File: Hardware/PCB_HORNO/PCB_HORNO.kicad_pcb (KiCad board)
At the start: 2 copper layers, 269 parts, among them J0_1 Screw_Terminal_01x03, J0_10 Screw_Terminal_01x03, J0_11 Screw_Terminal_01x03, J0_12 Screw_Terminal_01x03, J0_13 Screw_Terminal_01x03, J0_14 Screw_Terminal_01x03, J0_15 Screw_Terminal_01x03, J0_16 Screw_Terminal_01x03, J0_2 Screw_Terminal_01x03, J0_3 Screw_Terminal_01x03, J0_4 Screw_Terminal_01x03, J0_5 Screw_Terminal_01x03, J0_6 Screw_Terminal_01x03, J0_7 Screw_Terminal_01x03, J0_8 Screw_Terminal_01x03, J0_9 Screw_Terminal_01x03, J1 Screw_Terminal_01x20, J2 Screw_Terminal_01x20, J3 Screw_Terminal_01x20, J4 Screw_Terminal_01x20, J9_1 Screw_Terminal_01x03, J9_5 Screw_Terminal_01x03, Q1 2N2222, Q10 IRG4PF50W, Q2 2N2222, Q3 2N2222, Q4 2N2222, Q5 BTA16-800B, U1 TLP521-1, U10 LM741, U11 LM741, U12 LM741, U13 MOC3021M, U14 TLP521-1, U15 4069, U16 LM741, U17 LM741, U18 LM741, U19 TLP250, U2 TLP521-1, U20 L298HN, U21 4069, U3 TLP521-1, U4 TLP521-1, U5 TLP521-1, U6 TLP521-1, U7 TLP521-1, U8 TLP521-1, U9 LM741

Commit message: Esquematico listo
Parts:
- removed D9: D_Bridge_+-AA, Diode_THT:Diode_Bridge_19.0x3.5x10.0mm_P5.0mm
- removed the J0_14 at (-42.6, 357.2)
- removed the J0_14 at (243.4, 362.3)
- removed PX100, PX101, PX102, PX103, PX104, PX105, PX106, PX107, PX108, PX109, PX110, PX63, PX64, PX65, PX66, PX67, PX68, PX69, PX70, PX71, PX72, PX73, PX74, PX75, PX76, PX77, PX78, PX79, PX80, PX81, PX82, PX83, PX84, PX85, PX86, PX87, PX88, PX89, PX90, PX91, PX92, PX93, PX94, PX95, PX96, PX97, PX98, PX99: ~, Connector_Wire:SolderWire-0.75sqmm_1x01_D1.25mm_OD2.3mm
- removed U15, U21: 4069, Package_TO_SOT_SMD:SOT-353_SC-70-5
- added C10: 100nF, Capacitor_THT:C_Disc_D5.1mm_W3.2mm_P5.00mm, F.Cu at (152.8, 399.2)
- added C11: 100nF, Capacitor_THT:C_Disc_D5.1mm_W3.2mm_P5.00mm, F.Cu at (152.8, 404.0)
- added D10: GBU8J, Diode_THT:Diode_Bridge_Vishay_GBU, F.Cu at (-160.2, 414.6)
- added J0_14: Screw_Terminal_01x03, TerminalBlock_Phoenix:TerminalBlock_Phoenix_PT-1,5-3-3.5-H_1x03_P3.50mm_Horizontal, F.Cu at (247.8, 410.9)
- C1, C2, C3, C4, C5, C6, C7, C8, C9: footprint Capacitor_THT:C_Disc_D4.3mm_W1.9mm_P5.00mm -> Capacitor_THT:C_Disc_D5.1mm_W3.2mm_P5.00mm
- Q1, Q2, Q3, Q4: footprint Package_TO_SOT_THT:TO-39-3 -> Package_TO_SOT_THT:TO-92
- moved PX45 426.3 mm to (-314.9, 424.2)
- moved PX47 426.3 mm to (-314.9, 433.5)
- moved PX46 426.3 mm to (-314.9, 428.8)
- moved PX53 426.1 mm to (-305.2, 433.5)
- moved PX48 416.0 mm to (-310.1, 424.2)
- moved PX49 416.0 mm to (-310.1, 428.8)
- moved PX50 416.0 mm to (-310.1, 433.5)
- moved PX51 406.0 mm to (-305.2, 424.2)
- moved PX52 406.0 mm to (-305.2, 428.8)
- moved PX120 393.8 mm to (575.5, 400.5)
- moved PX121 393.8 mm to (575.5, 405.2)
- moved PX122 393.8 mm to (575.5, 409.8)
- moved PX123 393.8 mm to (575.5, 414.5)
- moved PX124 393.8 mm to (575.5, 419.1)
- moved PX54 286.0 mm to (-151.2, 420.0)
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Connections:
- C1 pad 1: unconnected-(C1-Pad1) -> Net-(3V3a1-Pin_1)
- C1 pad 2: unconnected-(C1-Pad2) -> Net-(GND1-Pin_1)
- C2 pad 1: unconnected-(C2-Pad1) -> Net-(3V3b1-Pin_1)
- C2 pad 2: unconnected-(C2-Pad2) -> Net-(GND3-Pin_1)
- C3 pad 1: Net-(J0_6-Pin_1) -> Net-(U12-+)
- C7 pad 1: Net-(U16-+) -> Net-(PX117-Pin_1)
- C7 pad 2: Net-(C7-Pad2) -> Net-(J0_12-Pin_3)
- C8 pad 1: Net-(U17-+) -> Net-(PX118-Pin_1)
- C8 pad 2: Net-(C7-Pad2) -> Net-(J0_12-Pin_3)
- C9 pad 1: Net-(U18-+) -> Net-(PX119-Pin_1)
- C9 pad 2: Net-(C7-Pad2) -> Net-(J0_12-Pin_3)
- J0_12 pad 2: unconnected-(J0_12-Pin_2-Pad2) -> Net-(J0_12-Pin_2)
- J0_6 pad 1: Net-(J0_6-Pin_1) -> unconnected-(J0_6-Pin_1-Pad1)
- J0_6 pad 2: unconnected-(J0_6-Pin_2-Pad2) -> Net-(J0_4-Pin_1)
- J0_6 pad 3: unconnected-(J0_6-Pin_3-Pad3) -> Net-(J0_4-Pin_1)
- PX111 pad 1: unconnected-(PX111-Pin_1-Pad1) -> Net-(PX111-Pin_1)
- PX112 pad 1: unconnected-(PX112-Pin_1-Pad1) -> Net-(PX112-Pin_1)
- PX113 pad 1: unconnected-(PX113-Pin_1-Pad1) -> Net-(PX113-Pin_1)
- PX114 pad 1: unconnected-(PX114-Pin_1-Pad1) -> Net-(PX114-Pin_1)
- PX115 pad 1: unconnected-(PX115-Pin_1-Pad1) -> Net-(PX115-Pin_1)
- PX116 pad 1: unconnected-(PX116-Pin_1-Pad1) -> Net-(J0_12-Pin_3)
- PX117 pad 1: unconnected-(PX117-Pin_1-Pad1) -> Net-(PX117-Pin_1)
- PX118 pad 1: unconnected-(PX118-Pin_1-Pad1) -> Net-(PX118-Pin_1)
- PX119 pad 1: unconnected-(PX119-Pin_1-Pad1) -> Net-(PX119-Pin_1)
- PX120 pad 1: unconnected-(PX120-Pin_1-Pad1) -> Net-(J0_4-Pin_1)
- PX121 pad 1: unconnected-(PX121-Pin_1-Pad1) -> Net-(PX121-Pin_1)
- PX122 pad 1: unconnected-(PX122-Pin_1-Pad1) -> Net-(PX122-Pin_1)
- PX123 pad 1: unconnected-(PX123-Pin_1-Pad1) -> Net-(PX123-Pin_1)
- PX124 pad 1: unconnected-(PX124-Pin_1-Pad1) -> Net-(PX124-Pin_1)
- PX45 pad 1: unconnected-(PX45-Pin_1-Pad1) -> Net-(J9_1-Pin_1)
- PX46 pad 1: unconnected-(PX46-Pin_1-Pad1) -> Net-(J9_1-Pin_1)
- PX47 pad 1: unconnected-(PX47-Pin_1-Pad1) -> Net-(PX47-Pin_1)
- PX48 pad 1: unconnected-(PX48-Pin_1-Pad1) -> Net-(PX48-Pin_1)
- PX49 pad 1: unconnected-(PX49-Pin_1-Pad1) -> Net-(PX49-Pin_1)
- PX50 pad 1: unconnected-(PX50-Pin_1-Pad1) -> Net-(PX50-Pin_1)
- PX51 pad 1: unconnected-(PX51-Pin_1-Pad1) -> Net-(PX51-Pin_1)
- PX52 pad 1: unconnected-(PX52-Pin_1-Pad1) -> Net-(PX52-Pin_1)
- PX53 pad 1: unconnected-(PX53-Pin_1-Pad1) -> Net-(PX53-Pin_1)
- PX54 pad 1: unconnected-(PX54-Pin_1-Pad1) -> Net-(PX54-Pin_1)
- PX55 pad 1: unconnected-(PX55-Pin_1-Pad1) -> Net-(J0_11-Pin_3)
- PX56 pad 1: unconnected-(PX56-Pin_1-Pad1) -> Net-(PX56-Pin_1)
- PX57 pad 1: unconnected-(PX57-Pin_1-Pad1) -> Net-(PX57-Pin_1)
- PX58 pad 1: unconnected-(PX58-Pin_1-Pad1) -> Net-(PX58-Pin_1)
- PX59 pad 1: unconnected-(PX59-Pin_1-Pad1) -> Net-(PX59-Pin_1)
- PX60 pad 1: unconnected-(PX60-Pin_1-Pad1) -> Net-(PX60-Pin_1)
- PX61 pad 1: unconnected-(PX61-Pin_1-Pad1) -> Net-(J0_16-Pin_1)
- PX62 pad 1: unconnected-(PX62-Pin_1-Pad1) -> Net-(PX62-Pin_1)
- Q1 pad 1: Net-(Q1-E) -> Net-(PX124-Pin_1)
- Q2 pad 1: Net-(Q2-E) -> Net-(PX123-Pin_1)
- Q3 pad 1: Net-(Q3-E) -> Net-(PX122-Pin_1)
- Q4 pad 1: Net-(Q4-E) -> Net-(PX121-Pin_1)
- R12 pad 1: Net-(R12-Pad1) -> Net-(J0_11-Pin_1)
- R12 pad 2: Net-(J0_11-Pin_3) -> Net-(PX54-Pin_1)
- R18 pad 1: unconnected-(R18-Pad1) -> Net-(PX57-Pin_1)
- R19 pad 2: Net-(C7-Pad2) -> Net-(J0_12-Pin_3)
- R2 pad 1: Net-(R2-Pad1) -> Net-(PX47-Pin_1)
- R21 pad 2: Net-(C7-Pad2) -> Net-(J0_12-Pin_3)
- R23 pad 2: Net-(C7-Pad2) -> Net-(J0_12-Pin_3)
- R25 pad 2: unconnected-(R25-Pad2) -> Net-(PX115-Pin_1)
- R3 pad 1: Net-(R3-Pad1) -> Net-(PX48-Pin_1)
- R35 pad 1: Net-(Q4-E) -> Net-(PX121-Pin_1)
- R36 pad 1: Net-(Q3-E) -> Net-(PX122-Pin_1)
- R37 pad 1: Net-(Q2-E) -> Net-(PX123-Pin_1)
- R38 pad 1: Net-(Q1-E) -> Net-(PX124-Pin_1)
- R39 pad 1: unconnected-(R39-Pad1) -> Net-(J0_16-Pin_1)
- R4 pad 1: Net-(R4-Pad1) -> Net-(PX49-Pin_1)
- R40 pad 1: unconnected-(R40-Pad1) -> Net-(J0_16-Pin_1)
- R5 pad 1: Net-(R5-Pad1) -> Net-(PX50-Pin_1)
- R6 pad 1: Net-(R6-Pad1) -> Net-(PX51-Pin_1)
- R7 pad 1: Net-(R7-Pad1) -> Net-(PX52-Pin_1)
- R8 pad 1: Net-(R8-Pad1) -> Net-(PX53-Pin_1)
- RV1 pad 1: unconnected-(RV1-Pad1) -> Net-(PX58-Pin_1)
- RV1 pad 2: unconnected-(RV1-Pad2) -> Net-(PX59-Pin_1)
- RV1 pad 3: unconnected-(RV1-Pad3) -> Net-(PX60-Pin_1)
- U12 pad 3: Net-(J0_6-Pin_1) -> Net-(U12-+)
- U13 pad 2: unconnected-(U13-Pad2) -> Net-(PX56-Pin_1)
- U14 pad 3: Net-(J0_11-Pin_1) -> Net-(J0_11-Pin_3)
- U14 pad 4: Net-(R12-Pad1) -> Net-(PX54-Pin_1)
- U16 pad 3: Net-(U16-+) -> Net-(PX117-Pin_1)
- U16 pad 4: Net-(J0_12-Pin_3) -> Net-(J0_12-Pin_1)
- U16 pad 7: Net-(J0_12-Pin_1) -> Net-(J0_12-Pin_2)
- U17 pad 3: Net-(U17-+) -> Net-(PX118-Pin_1)
- U17 pad 4: Net-(J0_12-Pin_3) -> Net-(J0_12-Pin_1)
- U17 pad 7: Net-(J0_12-Pin_1) -> Net-(J0_12-Pin_2)
- U18 pad 3: Net-(U18-+) -> Net-(PX119-Pin_1)
- U18 pad 4: Net-(J0_12-Pin_3) -> Net-(J0_12-Pin_1)
- U18 pad 7: Net-(J0_12-Pin_1) -> Net-(J0_12-Pin_2)
- U19 pad 3: unconnected-(U19-C-Pad3) -> Net-(PX114-Pin_1)
- U2 pad 3: Net-(R2-Pad1) -> Net-(PX47-Pin_1)
- U20 pad 10: Net-(U20-IN3) -> Net-(PX111-Pin_1)
- U20 pad 12: Net-(U20-IN4) -> Net-(PX62-Pin_1)
- U20 pad 5: Net-(U20-IN1) -> Net-(PX113-Pin_1)
- U20 pad 7: Net-(U20-IN2) -> Net-(PX112-Pin_1)
- U3 pad 3: Net-(R3-Pad1) -> Net-(PX48-Pin_1)
- U4 pad 3: Net-(R4-Pad1) -> Net-(PX49-Pin_1)
- U5 pad 3: Net-(R5-Pad1) -> Net-(PX50-Pin_1)
- U6 pad 3: Net-(R6-Pad1) -> Net-(PX51-Pin_1)
- U7 pad 3: Net-(R7-Pad1) -> Net-(PX52-Pin_1)
- U8 pad 3: Net-(R8-Pad1) -> Net-(PX53-Pin_1)

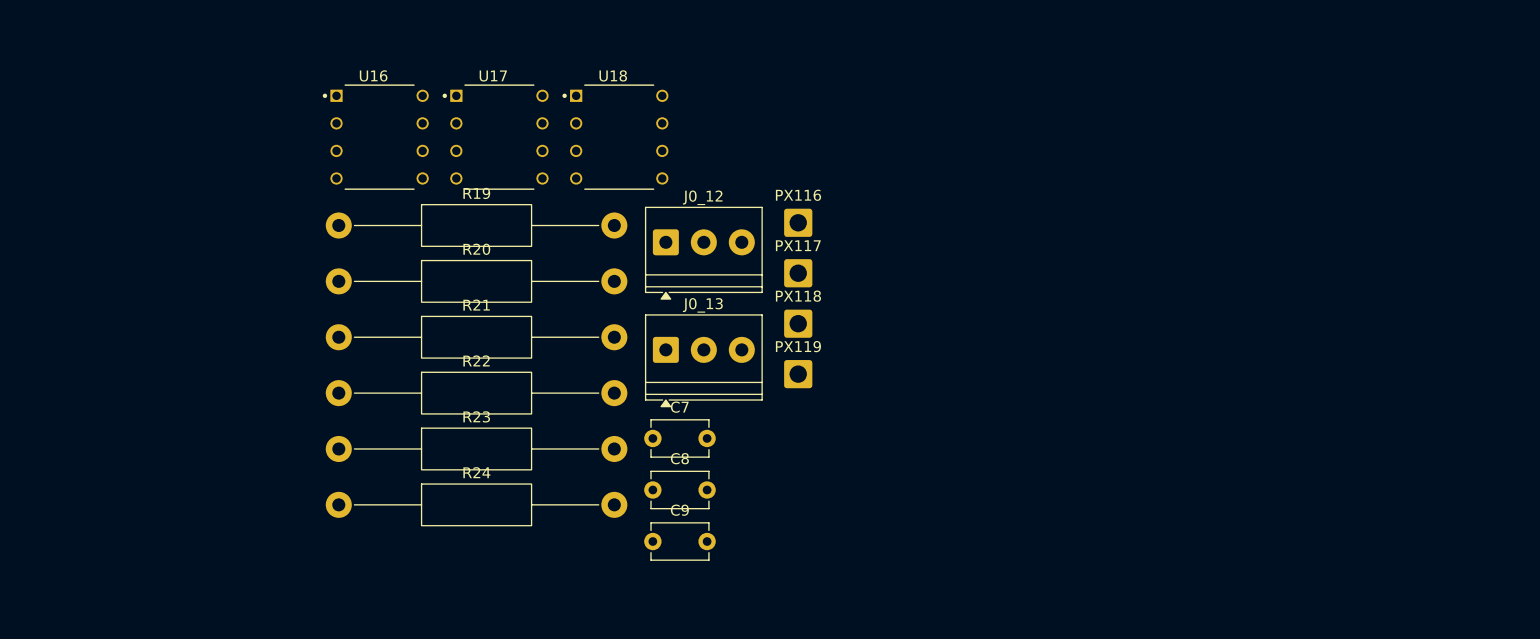
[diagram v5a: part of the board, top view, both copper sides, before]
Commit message: Reorganización del esquematico
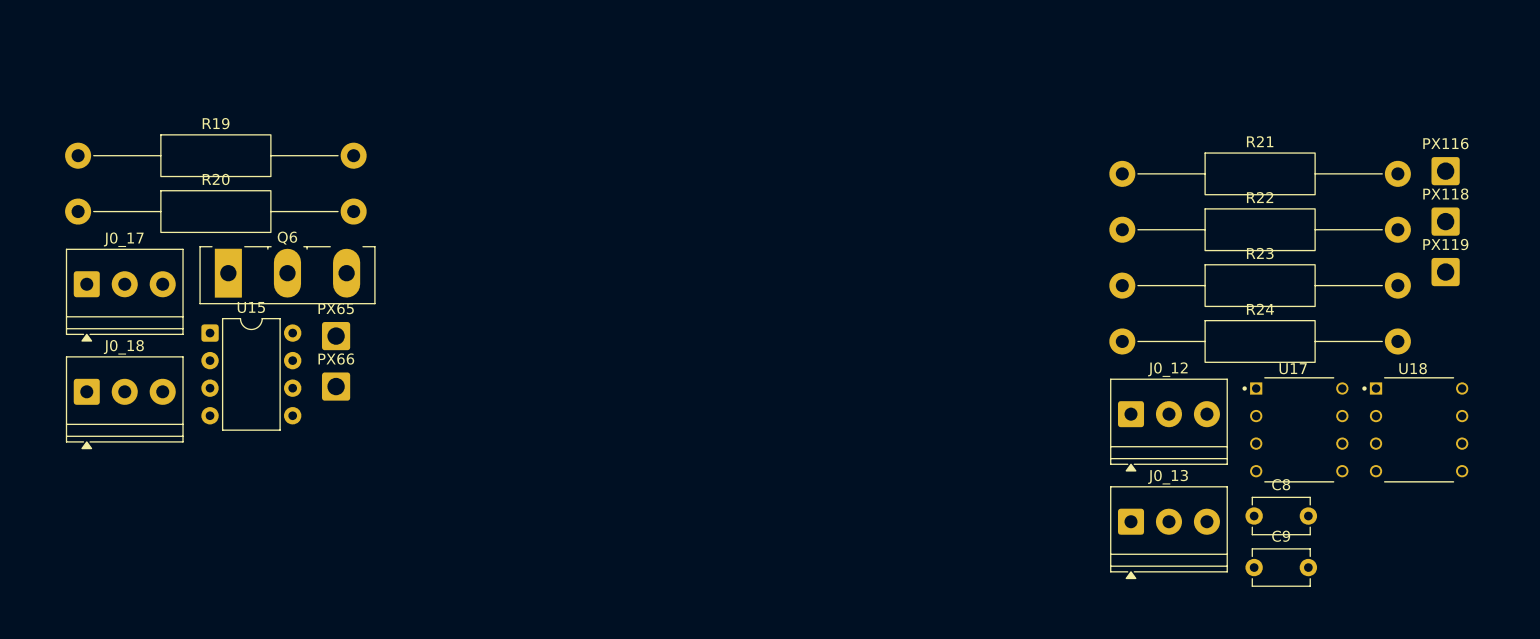
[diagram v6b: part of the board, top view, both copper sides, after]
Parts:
- removed C7: 10nF, Capacitor_THT:C_Disc_D5.1mm_W3.2mm_P5.00mm
- removed PX117: ~, Connector_Wire:SolderWire-0.75sqmm_1x01_D1.25mm_OD2.3mm
- removed U16: LM741, LM741_TH:LM471_TH
- added J0_17: Screw_Terminal_01x03, TerminalBlock_Phoenix:TerminalBlock_Phoenix_PT-1,5-3-3.5-H_1x03_P3.50mm_Horizontal, F.Cu at (340.4, 409.2)
- added J0_18: Screw_Terminal_01x03, TerminalBlock_Phoenix:TerminalBlock_Phoenix_PT-1,5-3-3.5-H_1x03_P3.50mm_Horizontal, F.Cu at (340.4, 419.1)
- added PX65: ~, Connector_Wire:SolderWire-0.75sqmm_1x01_D1.25mm_OD2.3mm, F.Cu at (363.4, 413.9)
- added PX66: ~, Connector_Wire:SolderWire-0.75sqmm_1x01_D1.25mm_OD2.3mm, F.Cu at (363.4, 418.6)
- added Q6: IRG4PF50W, Package_TO_SOT_THT:TO-247-3_Vertical, F.Cu at (353.5, 408.1)
- added U15: TLP250, Package_DIP:DIP-8_W7.62mm, F.Cu at (351.8, 413.7)
- moved U17 78.5 mm to (452.2, 422.6)
- moved U18 78.5 mm to (463.2, 422.6)
- moved R21 73.8 mm to (435.9, 399.0)
- moved R22 73.8 mm to (435.9, 404.1)
- moved R23 73.8 mm to (435.9, 409.3)
- moved R24 73.8 mm to (435.9, 414.4)
- moved PX118 60.4 mm to (465.7, 403.4)
- moved PX119 60.4 mm to (465.7, 408.0)
- moved PX116 59.9 mm to (465.7, 398.7)
- moved C8 55.5 mm to (448.0, 430.5)
- moved C9 55.5 mm to (448.0, 435.3)
- moved J0_12 45.7 mm to (436.7, 421.1)
- moved J0_13 45.7 mm to (436.7, 431.1)
- moved R19 24.9 mm to (339.6, 397.3)
- moved R20 24.9 mm to (339.6, 402.5)
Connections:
- C3 pad 1: Net-(U12-+) -> Net-(J0_6-Pin_1)
- C8 pad 2: Net-(J0_12-Pin_3) -> Net-(C8-Pad2)
- C9 pad 2: Net-(J0_12-Pin_3) -> Net-(C8-Pad2)
- J0_13 pad 2: Net-(J0_13-Pin_2) -> unconnected-(J0_13-Pin_2-Pad2)
- J0_6 pad 1: unconnected-(J0_6-Pin_1-Pad1) -> Net-(J0_6-Pin_1)
- R19 pad 1: Net-(U16--) -> Net-(Q6-G)
- R19 pad 2: Net-(J0_12-Pin_3) -> Net-(R19-Pad2)
- R20 pad 1: Net-(J0_13-Pin_3) -> Net-(U15-A)
- R20 pad 2: Net-(U16--) -> Net-(PX66-Pin_1)
- R21 pad 2: Net-(J0_12-Pin_3) -> Net-(C8-Pad2)
- R22 pad 1: Net-(J0_13-Pin_2) -> Net-(J0_13-Pin_3)
- R23 pad 2: Net-(J0_12-Pin_3) -> Net-(C8-Pad2)
- U12 pad 3: Net-(U12-+) -> Net-(J0_6-Pin_1)
- U17 pad 6: Net-(J0_13-Pin_2) -> Net-(J0_13-Pin_3)

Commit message: Organizando elementos en PCB
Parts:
- added J0_19: Screw_Terminal_01x03, TerminalBlock_Phoenix:TerminalBlock_Phoenix_PT-1,5-3-3.5-H_1x03_P3.50mm_Horizontal, F.Cu at (169.6, 323.4)
- added J0_20: Screw_Terminal_01x03, TerminalBlock_Phoenix:TerminalBlock_Phoenix_PT-1,5-3-3.5-H_1x03_P3.50mm_Horizontal, F.Cu at (153.9, 323.4)
- added PX63: ~, Connector_Wire:SolderWire-0.75sqmm_1x01_D1.25mm_OD2.3mm, F.Cu at (162.8, 261.2)
- added PX64: ~, Connector_Wire:SolderWire-0.75sqmm_1x01_D1.25mm_OD2.3mm, F.Cu at (158.2, 261.2)
- added PX67: ~, Connector_Wire:SolderWire-0.75sqmm_1x01_D1.25mm_OD2.3mm, F.Cu at (153.5, 261.2)
- added PX68: ~, Connector_Wire:SolderWire-0.75sqmm_1x01_D1.25mm_OD2.3mm, F.Cu at (176.8, 261.2)
- added PX69: ~, Connector_Wire:SolderWire-0.75sqmm_1x01_D1.25mm_OD2.3mm, F.Cu at (172.2, 261.2)
- added PX70: ~, Connector_Wire:SolderWire-0.75sqmm_1x01_D1.25mm_OD2.3mm, F.Cu at (167.5, 261.2)
- Q10, Q6: footprint Package_TO_SOT_THT:TO-247-3_Vertical -> Package_TO_SOT_THT:TO-264-3_Vertical
- RV1: value R_Potentiometer_US -> Potentiometer
- moved PX66 182.7 mm to (269.6, 261.8), turned to 90 degrees
- moved PX113 182.3 mm to (84.9, 261.3), turned to 90 degrees
- moved PX65 181.2 mm to (265.0, 261.8), turned to 90 degrees
- moved PX112 180.1 mm to (80.2, 261.3), turned to 90 degrees
- moved PX111 178.0 mm to (75.6, 261.3), turned to 90 degrees
- moved PX62 176.2 mm to (71.0, 261.3), turned to 90 degrees
- moved PX61 174.6 mm to (66.3, 261.3), turned to 90 degrees
- moved PX115 166.4 mm to (219.2, 262.1), turned to 90 degrees
- moved PX114 163.5 mm to (214.5, 262.1), turned to 90 degrees
- moved U20 157.1 mm to (98.6, 276.2), turned to -90 degrees
- moved PX60 156.7 mm to (13.0, 261.3), turned to -90 degrees
- moved PX57 155.8 mm to (-53.9, 261.3), turned to 90 degrees
- moved PX56 152.0 mm to (-58.5, 261.3), turned to 90 degrees
- moved PX59 151.5 mm to (17.6, 261.3), turned to -90 degrees
- moved PX58 146.3 mm to (22.3, 261.3), turned to -90 degrees
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
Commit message: Actualización de esquematico
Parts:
- removed J0_11, J0_12, J0_15, J0_17, J0_4, J9_1, J9_5: Screw_Terminal_01x03, TerminalBlock_Phoenix:TerminalBlock_Phoenix_PT-1,5-3-3.5-H_1x03_P3.50mm_Horizontal
- removed PX114, PX115: ~, Connector_Wire:SolderWire-0.75sqmm_1x01_D1.25mm_OD2.3mm
- removed Q10: IRG4PF50W, Package_TO_SOT_THT:TO-264-3_Vertical
- added J0_21: Screw_Terminal_01x03, TerminalBlock_Phoenix:TerminalBlock_Phoenix_PT-1,5-3-3.5-H_1x03_P3.50mm_Horizontal, F.Cu at (115.0, 427.5)
- added J0_22: Screw_Terminal_01x03, TerminalBlock_Phoenix:TerminalBlock_Phoenix_PT-1,5-3-3.5-H_1x03_P3.50mm_Horizontal, F.Cu at (115.0, 437.4)
- added J0_23: Screw_Terminal_01x03, TerminalBlock_Phoenix:TerminalBlock_Phoenix_PT-1,5-3-3.5-H_1x03_P3.50mm_Horizontal, F.Cu at (166.7, 428.5)
- added J0_24: Screw_Terminal_01x03, TerminalBlock_Phoenix:TerminalBlock_Phoenix_PT-1,5-3-3.5-H_1x03_P3.50mm_Horizontal, F.Cu at (166.7, 438.4)
- added J0_25: Screw_Terminal_01x03, TerminalBlock_Phoenix:TerminalBlock_Phoenix_PT-1,5-3-3.5-H_1x03_P3.50mm_Horizontal, F.Cu at (217.1, 428.0)
- added J0_26: Screw_Terminal_01x03, TerminalBlock_Phoenix:TerminalBlock_Phoenix_PT-1,5-3-3.5-H_1x03_P3.50mm_Horizontal, F.Cu at (217.1, 437.9)
- added K1: Fujitsu_FTR-LYCA005x, Relay_THT:Relay_SPDT_Fujitsu_FTR-LYCA005x_FormC_Vertical, F.Cu at (61.8, 409.0)
- added K2: Fujitsu_FTR-LYCA005x, Relay_THT:Relay_SPDT_Fujitsu_FTR-LYCA005x_FormC_Vertical, F.Cu at (114.0, 408.5)
- added K3: Fujitsu_FTR-LYCA005x, Relay_THT:Relay_SPDT_Fujitsu_FTR-LYCA005x_FormC_Vertical, F.Cu at (165.7, 409.5)
- added K4: Fujitsu_FTR-LYCA005x, Relay_THT:Relay_SPDT_Fujitsu_FTR-LYCA005x_FormC_Vertical, F.Cu at (216.1, 409.0)
- added PS1: MEE1S0315SC, Converter_DCDC:Converter_DCDC_Murata_MEE1SxxxxSC_THT, F.Cu at (288.0, 412.0)
- added PS2: MEE1S0315SC, Converter_DCDC:Converter_DCDC_Murata_MEE1SxxxxSC_THT, F.Cu at (295.8, 412.0)
- added PS3: MEE1S0315SC, Converter_DCDC:Converter_DCDC_Murata_MEE1SxxxxSC_THT, F.Cu at (357.2, 411.0)
- added PS4: MEE1S0315SC, Converter_DCDC:Converter_DCDC_Murata_MEE1SxxxxSC_THT, F.Cu at (365.0, 411.0)
- added PS5: MEE1S0315SC, Converter_DCDC:Converter_DCDC_Murata_MEE1SxxxxSC_THT, F.Cu at (-353.5, 434.5)
- added PS6: MEE1S0315SC, Converter_DCDC:Converter_DCDC_Murata_MEE1SxxxxSC_THT, F.Cu at (495.4, 305.4)
- added PS7: MEE1S0315SC, Converter_DCDC:Converter_DCDC_Murata_MEE1SxxxxSC_THT, F.Cu at (503.2, 305.4)
- added PS8: MEE1S0315SC, Converter_DCDC:Converter_DCDC_Murata_MEE1SxxxxSC_THT, F.Cu at (511.0, 305.4)
- added PX71: ~, Connector_Wire:SolderWire-0.75sqmm_1x01_D1.25mm_OD2.3mm, F.Cu at (229.3, 432.8)
- added PX72: ~, Connector_Wire:SolderWire-0.75sqmm_1x01_D1.25mm_OD2.3mm, F.Cu at (229.3, 437.5)
- added PX73: ~, Connector_Wire:SolderWire-0.75sqmm_1x01_D1.25mm_OD2.3mm, F.Cu at (283.5, 420.6)
- added PX74: ~, Connector_Wire:SolderWire-0.75sqmm_1x01_D1.25mm_OD2.3mm, F.Cu at (283.5, 425.2)
- added PX75: ~, Connector_Wire:SolderWire-0.75sqmm_1x01_D1.25mm_OD2.3mm, F.Cu at (283.5, 429.9)
- added PX76: ~, Connector_Wire:SolderWire-0.75sqmm_1x01_D1.25mm_OD2.3mm, F.Cu at (283.5, 434.5)
- added PX77: ~, Connector_Wire:SolderWire-0.75sqmm_1x01_D1.25mm_OD2.3mm, F.Cu at (352.7, 410.3)
- added PX78: ~, Connector_Wire:SolderWire-0.75sqmm_1x01_D1.25mm_OD2.3mm, F.Cu at (352.7, 414.9)
- added PX79: ~, Connector_Wire:SolderWire-0.75sqmm_1x01_D1.25mm_OD2.3mm, F.Cu at (352.7, 419.6)
- added PX80: ~, Connector_Wire:SolderWire-0.75sqmm_1x01_D1.25mm_OD2.3mm, F.Cu at (352.7, 424.2)
- added PX81: ~, Connector_Wire:SolderWire-0.75sqmm_1x01_D1.25mm_OD2.3mm, F.Cu at (352.7, 428.9)
- added PX82: ~, Connector_Wire:SolderWire-0.75sqmm_1x01_D1.25mm_OD2.3mm, F.Cu at (352.7, 433.5)
- added PX83: ~, Connector_Wire:SolderWire-0.75sqmm_1x01_D1.25mm_OD2.3mm, F.Cu at (490.9, 304.8)
- added PX84: ~, Connector_Wire:SolderWire-0.75sqmm_1x01_D1.25mm_OD2.3mm, F.Cu at (490.9, 309.4)
- added PX85: ~, Connector_Wire:SolderWire-0.75sqmm_1x01_D1.25mm_OD2.3mm, F.Cu at (-345.3, 433.9)
- added PX86: ~, Connector_Wire:SolderWire-0.75sqmm_1x01_D1.25mm_OD2.3mm, F.Cu at (-345.3, 438.5)
- added PX87: ~, Connector_Wire:SolderWire-0.75sqmm_1x01_D1.25mm_OD2.3mm, F.Cu at (490.9, 314.1)
- added PX88: ~, Connector_Wire:SolderWire-0.75sqmm_1x01_D1.25mm_OD2.3mm, F.Cu at (490.9, 318.7)
- added PX89: ~, Connector_Wire:SolderWire-0.75sqmm_1x01_D1.25mm_OD2.3mm, F.Cu at (490.9, 323.4)
- added PX90: ~, Connector_Wire:SolderWire-0.75sqmm_1x01_D1.25mm_OD2.3mm, F.Cu at (490.9, 328.0)
- added Q7: IRG4PF50W, Package_TO_SOT_THT:TO-264-3_Vertical, F.Cu at (360.5, 424.2)
- added R41: R_US, Resistor_THT:R_Axial_DIN0411_L9.9mm_D3.6mm_P25.40mm_Horizontal, F.Cu at (62.0, 416.1)
- added R42: R_US, Resistor_THT:R_Axial_DIN0411_L9.9mm_D3.6mm_P25.40mm_Horizontal, F.Cu at (62.0, 421.3)
- added R43: R_US, Resistor_THT:R_Axial_DIN0411_L9.9mm_D3.6mm_P25.40mm_Horizontal, F.Cu at (114.2, 415.6)
- added R44: R_US, Resistor_THT:R_Axial_DIN0411_L9.9mm_D3.6mm_P25.40mm_Horizontal, F.Cu at (114.2, 420.8)
- added R45: R_US, Resistor_THT:R_Axial_DIN0411_L9.9mm_D3.6mm_P25.40mm_Horizontal, F.Cu at (165.9, 416.6)
- added R46: R_US, Resistor_THT:R_Axial_DIN0411_L9.9mm_D3.6mm_P25.40mm_Horizontal, F.Cu at (165.9, 421.8)
- added R47: R_US, Resistor_THT:R_Axial_DIN0411_L9.9mm_D3.6mm_P25.40mm_Horizontal, F.Cu at (216.3, 416.1)
- added R48: R_US, Resistor_THT:R_Axial_DIN0411_L9.9mm_D3.6mm_P25.40mm_Horizontal, F.Cu at (216.3, 421.3)
- added R49: R_US, Resistor_THT:R_Axial_DIN0411_L9.9mm_D3.6mm_P25.40mm_Horizontal, F.Cu at (-321.6, 374.7)
- added U16: TLP521-1, Package_DIP:DIP-4_W7.62mm, F.Cu at (74.2, 425.9)
- added U21: TLP521-1, Package_DIP:DIP-4_W7.62mm, F.Cu at (126.4, 425.4)
- added U22: TLP521-1, Package_DIP:DIP-4_W7.62mm, F.Cu at (178.1, 426.4)
- added U23: TLP521-1, Package_DIP:DIP-4_W7.62mm, F.Cu at (228.5, 425.9)
- RV1: value Potentiometer -> R_Potentiometer_US
- moved PX69 201.3 mm to (75.0, 437.5), turned to 0 degrees
- moved PX68 199.6 mm to (75.0, 432.8), turned to 0 degrees
- moved U19 190.5 mm to (372.3, 410.0), turned to 0 degrees
- moved PX70 180.4 mm to (127.2, 437.0), turned to 0 degrees
- moved PX67 178.6 mm to (178.9, 438.0), turned to 0 degrees
- moved PX63 174.8 mm to (127.2, 432.3), turned to 0 degrees
- moved PX64 173.4 mm to (178.9, 433.3), turned to 0 degrees
- moved R25 171.9 mm to (352.3, 400.2), turned to 0 degrees
- moved R26 166.7 mm to (352.3, 405.4), turned to 0 degrees
- moved PX66 154.8 mm to (283.5, 415.9), turned to 0 degrees
- moved PX65 150.6 mm to (283.5, 411.3), turned to 0 degrees
- moved J0_19 149.5 mm to (62.8, 428.0)
- moved J0_14 147.8 mm to (357.9, 432.2)
- moved J0_20 146.3 mm to (62.8, 437.9)
- moved U15 119.6 mm to (303.1, 411.0), turned to 0 degrees
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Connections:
- C3 pad 2: Net-(J0_4-Pin_1) -> Net-(J0_6-Pin_2)
- C4 pad 2: Net-(J0_4-Pin_1) -> Net-(J0_6-Pin_2)
- C5 pad 2: Net-(J0_4-Pin_1) -> Net-(J0_6-Pin_2)
- C6 pad 2: Net-(J0_4-Pin_1) -> Net-(J0_6-Pin_2)
- C8 pad 2: Net-(C8-Pad2) -> Net-(J0_6-Pin_2)
- C9 pad 2: Net-(C8-Pad2) -> Net-(J0_6-Pin_2)
- J0_14 pad 2: Net-(J0_14-Pin_2) -> unconnected-(J0_14-Pin_2-Pad2)
- J0_20 pad 2: Net-(J0_20-Pin_2) -> unconnected-(J0_20-Pin_2-Pad2)
- J0_6 pad 2: Net-(J0_4-Pin_1) -> Net-(J0_6-Pin_2)
- J0_6 pad 3: Net-(J0_4-Pin_1) -> Net-(J0_6-Pin_2)
- PX116 pad 1: Net-(J0_12-Pin_3) -> Net-(J0_6-Pin_2)
- PX120 pad 1: Net-(J0_4-Pin_1) -> Net-(J0_6-Pin_2)
- PX45 pad 1: Net-(J9_1-Pin_1) -> Net-(PS5--Vout)
- PX46 pad 1: Net-(J9_1-Pin_1) -> Net-(PS5--Vout)
- PX55 pad 1: Net-(J0_11-Pin_3) -> Net-(PS5--Vout)
- PX63 pad 1: Net-(J0_20-Pin_3) -> Net-(PX63-Pin_1)
- PX64 pad 1: Net-(J0_20-Pin_2) -> Net-(PX64-Pin_1)
- PX67 pad 1: Net-(J0_20-Pin_1) -> Net-(PX67-Pin_1)
- PX68 pad 1: Net-(J0_19-Pin_3) -> Net-(PX68-Pin_1)
- PX69 pad 1: Net-(J0_19-Pin_2) -> Net-(PX69-Pin_1)
- PX70 pad 1: Net-(J0_19-Pin_1) -> Net-(PX70-Pin_1)
- R1 pad 1: Net-(J9_1-Pin_1) -> Net-(PS5--Vout)
- R1 pad 2: Net-(J9_1-Pin_1) -> Net-(PS5--Vout)
- R2 pad 2: Net-(J9_1-Pin_1) -> Net-(PS5--Vout)
- R21 pad 2: Net-(C8-Pad2) -> Net-(J0_6-Pin_2)
- R23 pad 2: Net-(C8-Pad2) -> Net-(J0_6-Pin_2)
- R25 pad 1: Net-(U19-A) -> Net-(Q7-G)
- R25 pad 2: Net-(PX115-Pin_1) -> Net-(R25-Pad2)
- R26 pad 1: Net-(Q10-G) -> Net-(U19-A)
- R26 pad 2: Net-(R26-Pad2) -> Net-(PX80-Pin_1)
- R3 pad 2: Net-(J9_1-Pin_1) -> Net-(PS5--Vout)
- R35 pad 2: Net-(J0_4-Pin_1) -> Net-(J0_6-Pin_2)
- R36 pad 2: Net-(J0_4-Pin_1) -> Net-(J0_6-Pin_2)
- R37 pad 2: Net-(J0_4-Pin_1) -> Net-(J0_6-Pin_2)
- R38 pad 2: Net-(J0_4-Pin_1) -> Net-(J0_6-Pin_2)
- R4 pad 2: Net-(J9_1-Pin_1) -> Net-(PS5--Vout)
- R5 pad 2: Net-(J9_1-Pin_1) -> Net-(PS5--Vout)
- R6 pad 2: Net-(J9_1-Pin_1) -> Net-(PS5--Vout)
- R7 pad 2: Net-(J9_1-Pin_1) -> Net-(PS5--Vout)
- R8 pad 2: Net-(J9_1-Pin_1) -> Net-(PS5--Vout)
- U1 pad 3: Net-(J9_1-Pin_1) -> Net-(PS5--Vout)
- U10 pad 4: Net-(J0_4-Pin_2) -> Net-(PS7--Vout)
- U10 pad 7: Net-(J0_4-Pin_3) -> Net-(PS6-+Vout)
- U11 pad 4: Net-(J0_4-Pin_2) -> Net-(PS7--Vout)
- U11 pad 7: Net-(J0_4-Pin_3) -> Net-(PS6-+Vout)
- U12 pad 4: Net-(J0_4-Pin_2) -> Net-(PS7--Vout)
- U12 pad 7: Net-(J0_4-Pin_3) -> Net-(PS6-+Vout)
- U14 pad 3: Net-(J0_11-Pin_3) -> Net-(PS5--Vout)
- U17 pad 4: Net-(J0_12-Pin_1) -> Net-(PS7--Vout)
- U17 pad 7: Net-(J0_12-Pin_2) -> Net-(PS6-+Vout)
- U18 pad 4: Net-(J0_12-Pin_1) -> Net-(PS7--Vout)
- U18 pad 7: Net-(J0_12-Pin_2) -> Net-(PS6-+Vout)
- U19 pad 5: Net-(J0_14-Pin_3) -> Net-(PS3--Vout)
- U19 pad 7: Net-(R26-Pad2) -> Net-(R25-Pad2)
- U19 pad 8: Net-(J0_14-Pin_1) -> Net-(PS4-+Vout)
- U9 pad 4: Net-(J0_4-Pin_2) -> Net-(PS7--Vout)
- U9 pad 7: Net-(J0_4-Pin_3) -> Net-(PS6-+Vout)
